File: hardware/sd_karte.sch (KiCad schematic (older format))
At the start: 11 parts, among them CON1 SD_Card

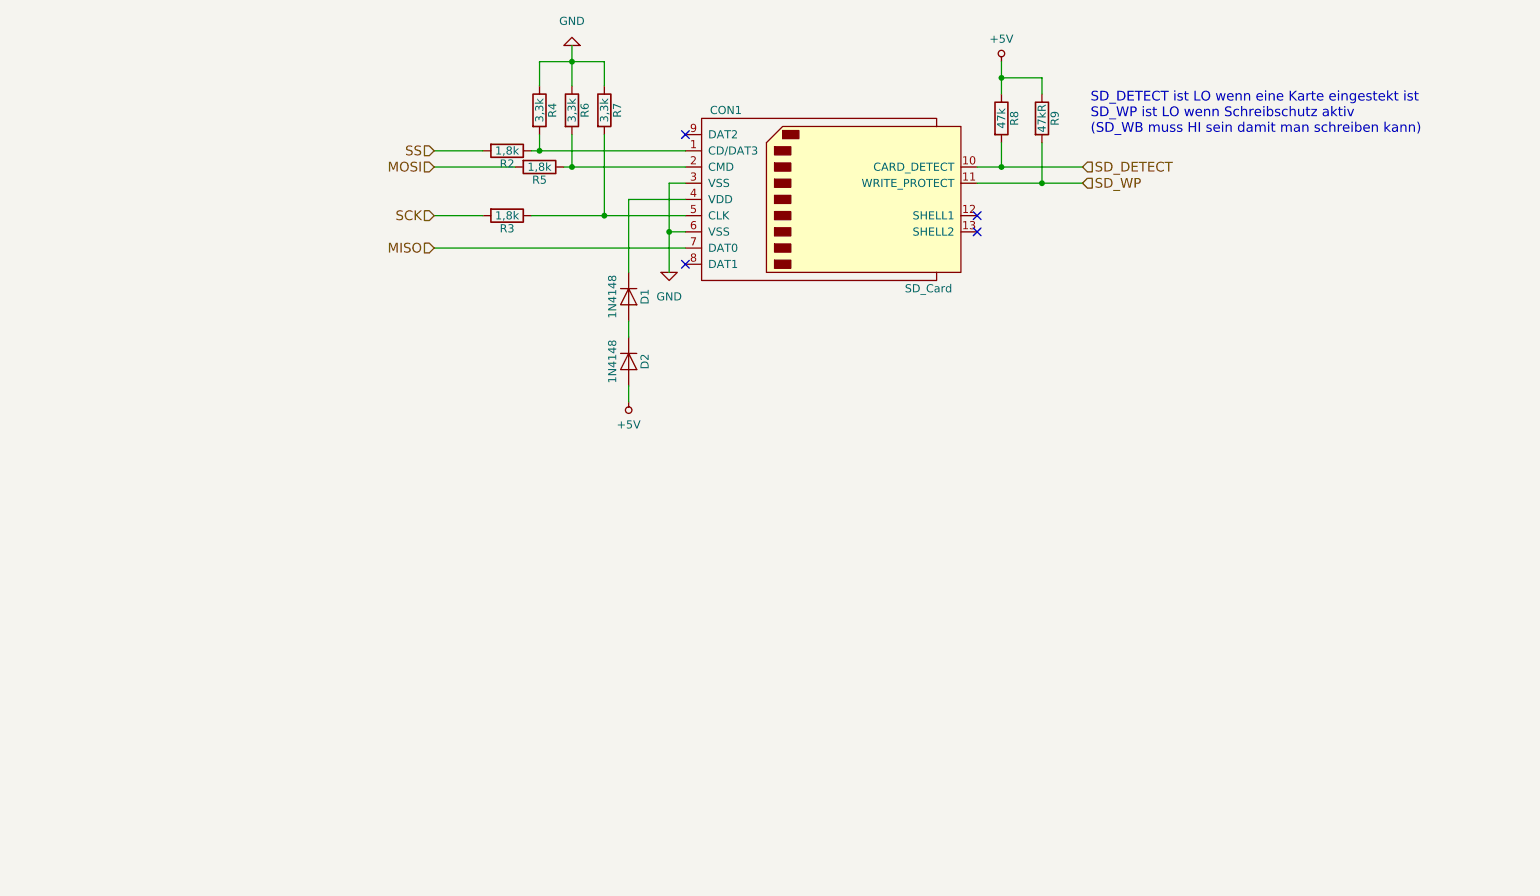
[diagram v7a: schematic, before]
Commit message: Jumper für EXT_5V hinzugefügt. Schaltplan aufgeräumt. Schaltplan auf Revision 1.3.3 gesetzt.
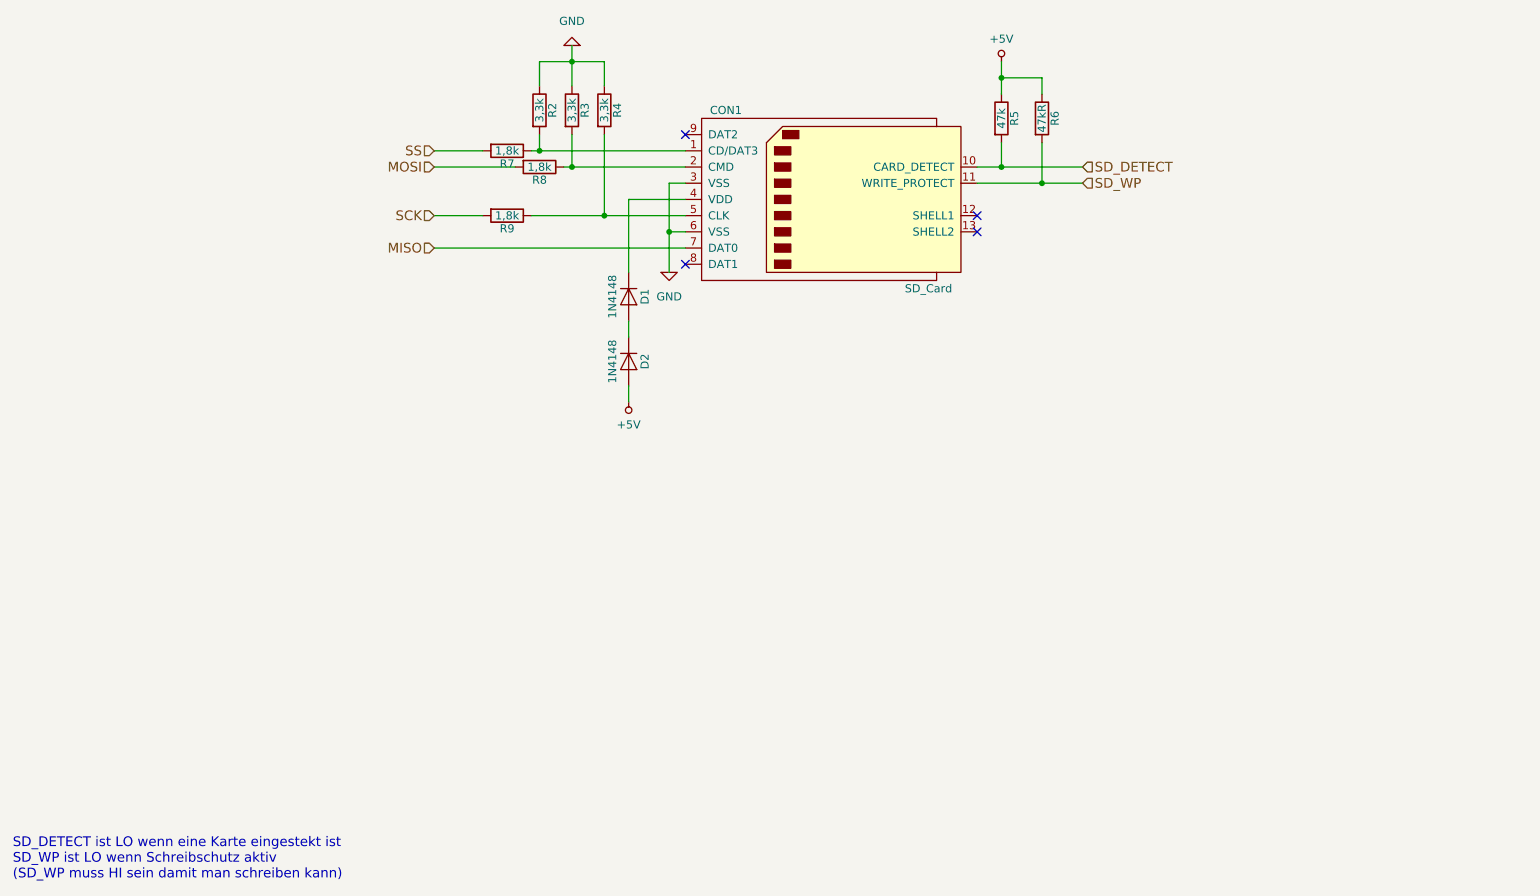
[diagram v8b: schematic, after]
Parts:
- renumbered R4 to R2, R6 to R3, R7 to R4, R8 to R5, R9 to R6, R2 to R7, R5 to R8, R3 to R9
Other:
- note added: "SD_DETECT ist LO wenn eine Karte eingestekt ist\nSD_WP ist LO wenn Schreibschutz aktiv\n(SD_WP muss HI sein damit man schreiben kann)"
- note removed: "SD_DETECT ist LO wenn eine Karte eingestekt ist\nSD_WP ist LO wenn Schreibschutz aktiv\n(SD_WB muss HI sein damit man schreiben kann)"
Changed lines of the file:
@@
 Title "1541-rebuid"
 Date "2018-05-06"
-Rev "1.3.2"
+Rev "1.3.3"
 Comp ""
 Comment1 "Erstellt: von: Thorsten Kattanek"
@@
 $EndComp
 $Comp
-L GND #PWR14
+L GND #PWR16
 U 1 1 55F7A326
 P 4700 3900
-F 0 "#PWR14" H 4700 3650 50  0001 C CNN
+F 0 "#PWR16" H 4700 3650 50  0001 C CNN
 F 1 "GND" H 4700 3750 50  0000 C CNN
 F 2 "" H 4700 3900 60  0000 C CNN
@@
 $EndComp
 $Comp
-L +5V #PWR13
+L +5V #PWR17
 U 1 1 55F7A887
 P 4450 4700
-F 0 "#PWR13" H 4450 4550 50  0001 C CNN
+F 0 "#PWR17" H 4450 4550 50  0001 C CNN
 F 1 "+5V" H 4450 4840 50  0000 C CNN
 F 2 "" H 4450 4700 60  0000 C CNN
@@
 NoConn ~ 4800 3050
 $Comp
-L R R2
+L R R7
 U 1 1 55F7B36C
 P 3700 3150
-F 0 "R2" V 3780 3150 50  0000 C CNN
+F 0 "R7" V 3780 3150 50  0000 C CNN
 F 1 "1,8k" V 3700 3150 50  0000 C CNN
 F 2 "Resistors_ThroughHole:Resistor_Horizontal_RM10mm" V 3630 3150 30  0001 C CNN
@@
 $EndComp
 $Comp
-L R R5
+L R R8
 U 1 1 55F7B401
 P 3900 3250
-F 0 "R5" V 3980 3250 50  0000 C CNN
+F 0 "R8" V 3980 3250 50  0000 C CNN
 F 1 "1,8k" V 3900 3250 50  0000 C CNN
 F 2 "Resistors_ThroughHole:Resistor_Horizontal_RM10mm" V 3830 3250 30  0001 C CNN
@@
 $EndComp
 $Comp
-L R R3
+L R R9
 U 1 1 55F7B48C
 P 3700 3550
-F 0 "R3" V 3780 3550 50  0000 C CNN
+F 0 "R9" V 3780 3550 50  0000 C CNN
 F 1 "1,8k" V 3700 3550 50  0000 C CNN
 F 2 "Resistors_ThroughHole:Resistor_Horizontal_RM10mm" V 3630 3550 30  0001 C CNN
@@
 $EndComp
 $Comp
-L R R4
+L R R2
 U 1 1 55F7BA6C
 P 3900 2900
-F 0 "R4" V 3980 2900 50  0000 C CNN
+F 0 "R2" V 3980 2900 50  0000 C CNN
 F 1 "3,3k" V 3900 2900 50  0000 C CNN
 F 2 "Resistors_ThroughHole:Resistor_Horizontal_RM10mm" V 3830 2900 30  0001 C CNN
@@
 $EndComp
 $Comp
-L R R6
+L R R3
 U 1 1 55F7BC20
 P 4100 2900
-F 0 "R6" V 4180 2900 50  0000 C CNN
+F 0 "R3" V 4180 2900 50  0000 C CNN
 F 1 "3,3k" V 4100 2900 50  0000 C CNN
 F 2 "Resistors_ThroughHole:Resistor_Horizontal_RM10mm" V 4030 2900 30  0001 C CNN
@@
 $EndComp
 $Comp
-L R R7
+L R R4
 U 1 1 55F7BCCD
 P 4300 2900
-F 0 "R7" V 4380 2900 50  0000 C CNN
+F 0 "R4" V 4380 2900 50  0000 C CNN
 F 1 "3,3k" V 4300 2900 50  0000 C CNN
 F 2 "Resistors_ThroughHole:Resistor_Horizontal_RM10mm" V 4230 2900 30  0001 C CNN
@@
 $EndComp
 $Comp
-L GND #PWR12
+L GND #PWR14
 U 1 1 55F7BE30
 P 4100 2500
-F 0 "#PWR12" H 4100 2250 50  0001 C CNN
+F 0 "#PWR14" H 4100 2250 50  0001 C CNN
 F 1 "GND" H 4100 2350 50  0000 C CNN
 F 2 "" H 4100 2500 60  0000 C CNN
@@
 Connection ~ 4700 3650
 $Comp
-L R R8
+L R R5
 U 1 1 5ADB73A5
 P 6750 2950
-F 0 "R8" V 6830 2950 50  0000 C CNN
+F 0 "R5" V 6830 2950 50  0000 C CNN
 F 1 "47k" V 6750 2950 50  0000 C CNN
 F 2 "" V 6680 2950 50  0001 C CNN
@@
 $EndComp
 $Comp
-L R R9
+L R R6
 U 1 1 5ADB753C
 P 7000 2950
-F 0 "R9" V 7080 2950 50  0000 C CNN
+F 0 "R6" V 7080 2950 50  0000 C CNN
 F 1 "47kR" V 7000 2950 50  0000 C CNN
 F 2 "" V 6930 2950 50  0001 C CNN
@@
 	7000 3100 7000 3350
 Connection ~ 7000 3350
-Text Notes 7300 3050 0    60   ~ 0
-SD_DETECT ist LO wenn eine Karte eingestekt ist\nSD_WP ist LO wenn Schreibschutz aktiv\n(SD_WB muss HI sein damit man schreiben kann)
+Text Notes 650  7650 0    60   ~ 0
+SD_DETECT ist LO wenn eine Karte eingestekt ist\nSD_WP ist LO wenn Schreibschutz aktiv\n(SD_WP muss HI sein damit man schreiben kann)
 $EndSCHEMATC
